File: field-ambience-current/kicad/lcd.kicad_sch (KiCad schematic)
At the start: 22 parts, among them J9 JST PH 2.0 2-pin (LiPo Batter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, Q1 DMG2305UX P-MOS SOT-23 (USB-C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, U7 MCP73831T-2ACI/OT (LiPo Charg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, U8 TPS61089RNR (Boost LiPo→5V, 2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

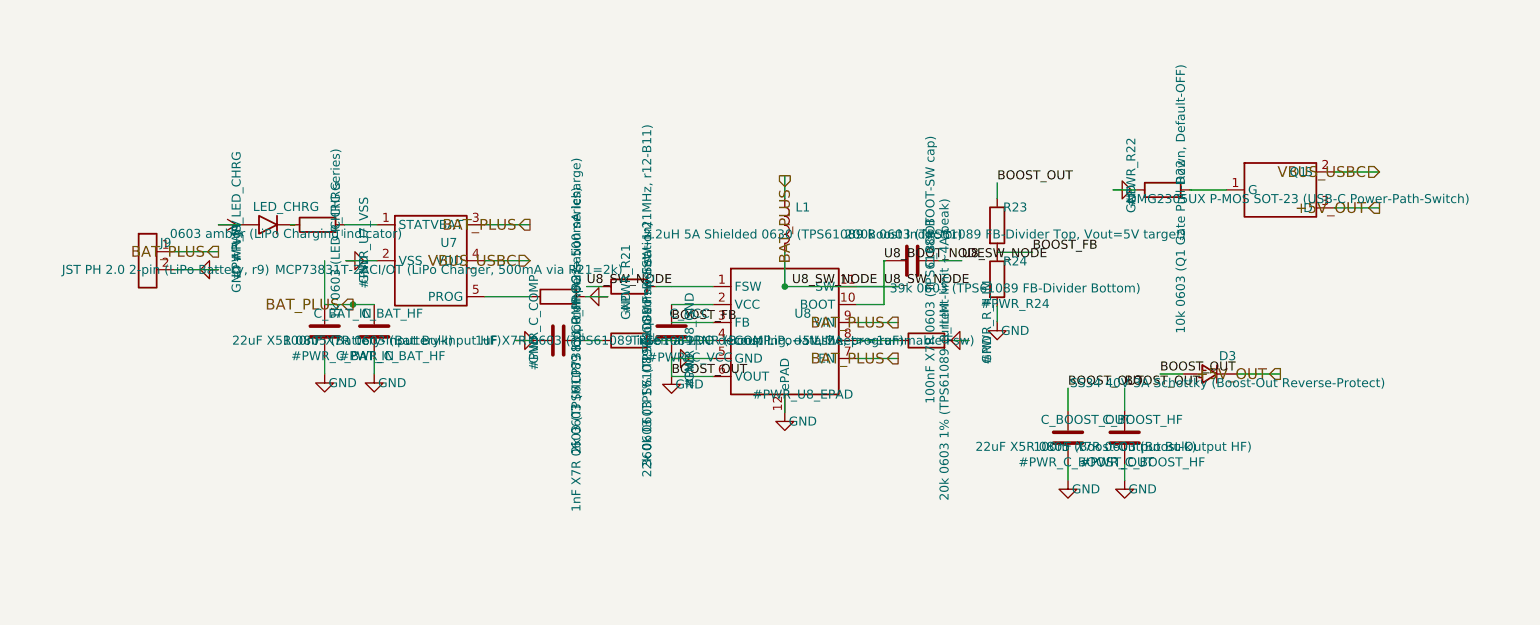
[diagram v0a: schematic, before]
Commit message: pcb(r18.5): Schematic-Migration Phase 3 — STM32H743 + LCD im Generator, Repo-Audit-Fixes
KERN: generate_kicad_project.py erzeugt jetzt die H7-Architektur.

NEU stm32h743.kicad_sch (ersetzt pico.kicad_sch -> kicad/legacy_pico2/):
- 100-Pin-Symbol 1:1 aus offizieller KiCad-Lib (MCU_ST_STM32H7),
  doppelt verifiziert gegen SPEC v0.7 §5 / DS12110 Rev 5 Table 8 —
  alle 52 belegten Zuordnungen identisch (zwei unabhängige Quellen)
- alle SPEC-§5-Netze verdrahtet, 48 Reserve-GPIOs no_connect
- Support: HSE Y1 ABLS-8.000MHZ-B4-T (C596838) + 2x22pF, VCAP 2x2.2uF
  (DS12110 Tab.24), 5x(4.7uF+100nF) VDD-Bank, VDDA-Ferrit C84094 +
  1uF+100nF, BOOT0-PD 10k, NRST-PU 10k+100nF, SWD-J4 (PA13/PA14/GND),
  BAT-Teiler 100k/100k+10nF an PA3, Status-LED PD8, USB-FS PA11/PA12
  (USBLC6-ESD bleibt davor), MIDI_TX-Netz (PD5)

NEU lcd.kicad_sch (ersetzt oled.kicad_sch -> legacy): 8-Pin-ST7789
per SPEC §6 + C6b/C6c + Backlight: PCA9685-Kanal-12 -> LCD_BLK_PWM ->
2N7002 Low-Side + 100k-PD. Netze OLED_* -> LCD_*.

power_tree: U5 AP7361A-33 LDO (+5V->+3V3) + Cin 1uF/Cout 2.2uF +
EN->IN. Pico-SMPS entfällt. PICO_USB_* -> USB_DM/USB_DP.

mcp: GPB5 = VOL_SW (SPEC §5.4 — lag bis r17 entgegen der SPEC am
Pico-GPIO), PCA-Kanal 12 = LCD_BLK_PWM. Root-Brücken umgebaut,
kicad_pro-Sheetliste: Battery ergänzt (fehlte).

AUDIT-FINDINGS (verifiziert, nicht aus dem Alt-Audit übernommen):
- F-6 NEU 🔴: SPEC-§4-U5-LCSC C156144 ist ein 910R-WIDERSTAND
  (LCSC-Web verifiziert) — hätte bei JLC einen R als LDO bestückt.
  SPEC korrigiert (Kandidat C150719), Symbol trägt TBD-VERIFY.
- B-LDO 🔴: AP7361A-SOT-89-5-Pinout-Annahme (1=ADJ/NC,2=OUT,3=IN,
  4=GND,5=EN aus AP7361-DS33626-Lesart; A-Datasheet war HTTP 403) —
  als PIN_VERIFY am Symbol + PCB_LAYOUT_STATUS dokumentiert.
- B-SW12 🔴: SW6-10 (HX 12x12) auf ~6mm-TL3342-Pattern — als
  FP_MISMATCH-Property an allen 5 Symbolen markiert.
- F-2-Teilfix: Encoder-MPN -> EC11J1525402, Bourns-PEC11R-PDF nach
  datasheets/legacy/ (falsches Teil); ALPS-Drawing offen.
- F-1: T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
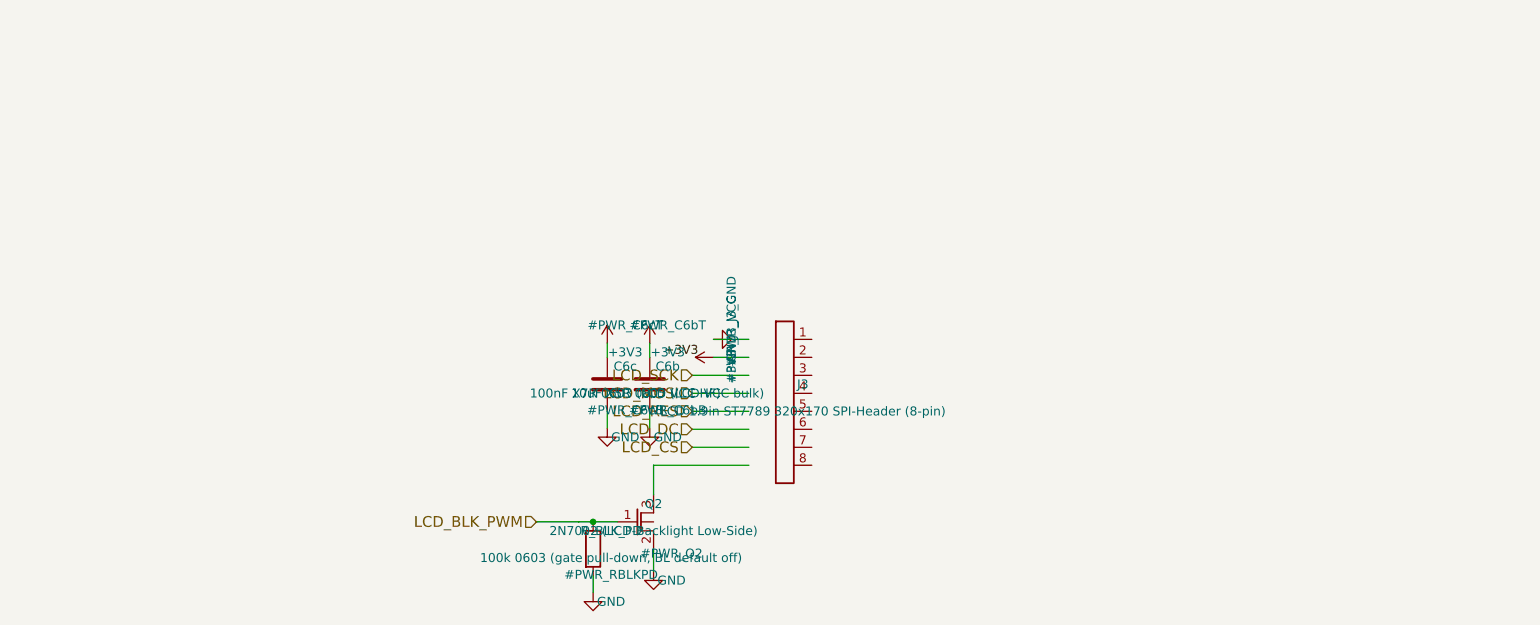
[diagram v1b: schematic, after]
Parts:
- removed C_BAT_HF: 100nF X7R 0603 (Battery-Input HF), Capacitor_SMD:C_0603_1608Metric, symbol Device:C
- removed C_BAT_IN: 22uF X5R 0805 (Battery-Input Bulk), Capacitor_SMD:C_0805_2012Metric, symbol Device:C
- removed C_BOOST_HF: 100nF X7R 0603 (Boost-Output HF), Capacitor_SMD:C_0603_1608Metric, symbol Device:C
- removed C_BOOST_OUT: 22uF X5R 0805 (Boost-Output Bulk), Capacitor_SMD:C_0805_2012Metric, symbol Device:C
- removed C_BOOT: 100nF X7R 0603 (TPS61089 BOOT-SW cap), Capacitor_SMD:C_0603_1608Metric, symbol Device:C
- removed C_COMP: 1nF X7R 0603 (TPS61089 loop-compensation series), Capacitor_SMD:C_0603_1608Metric, symbol Device:C
- removed C_VCC: 1uF X7R 0603 (TPS61089 internal LDO decoupling, d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, Capacitor_SMD:C_0603_1608Metric, symbol Device:C
- removed D3: SS34 40V 3A Schottky (Boost-Out Reverse-Protect), Diode_SMD:D_SMA, symbol Device:D_Schottky
- removed J9: JST PH 2.0 2-pin (LiPo Battery, r9), Connector_JST:JST_PH_S2B-PH-SM4-TB_1x02-1MP_P2.00mm_Horizontal, symbol Connector:Conn_01x02
- removed L1: 2.2uH 5A Shielded 0630 (TPS61089 Boost Inductor), Inductor_SMD:L_0630_6.0x6.0mm, symbol Device:L
- removed LED_CHRG: 0603 amber (LiPo Charging indicator), LED_SMD:LED_0603_1608Metric, symbol Device:LED
- removed Q1: DMG2305UX P-MOS SOT-23 (USB-C Power-Path-Switch), Package_TO_SOT_SMD:SOT-23, symbol Transistor_FET:DMG2305UX
- removed R21: 2k 0603 (MCP73831 R_PROG → 500mA Icharge), Resistor_SMD:R_0603_1608Metric, symbol Device:R
- removed R22: 10k 0603 (Q1 Gate Pull-Down, Default-OFF), Resistor_SMD:R_0603_1608Metric, symbol Device:R
- removed R23: 200k 0603 (TPS61089 FB-Divider Top, Vout=5V targe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, Resistor_SMD:R_0603_1608Metric, symbol Device:R
- removed R24: 39k 0603 (TPS61089 FB-Divider Bottom), Resistor_SMD:R_0603_1608Metric, symbol Device:R
- removed R_CHRG: 1k 0603 (LED_CHRG series), Resistor_SMD:R_0603_1608Metric, symbol Device:R
- removed R_COMP: 22k 0603 (TPS61089 loop-compensation), Resistor_SMD:R_0603_1608Metric, symbol Device:R
- removed R_FSW: 360k 0603 1% (TPS61089 Fsw-Set ~1.21MHz, r12-B11), Resistor_SMD:R_0603_1608Metric, symbol Device:R
- removed R_ILIM: 20k 0603 1% (TPS61089 current-limit ~4A peak), Resistor_SMD:R_0603_1608Metric, symbol Device:R
- removed U7: MCP73831T-2ACI/OT (LiPo Charger, 500mA via R21=2k), Package_TO_SOT_SMD:SOT-23-5, symbol Battery:MCP73831
- removed U8: TPS61089RNR (Boost LiPo→5V, 2A, programmable Fsw), Package_DFN_QFN:VQFN-11-1EP_2.6x2.6mm_P0.5mm_EP0.85x1.5mm_HotRod, symbol Regulator_Switching:TPS61089
- added C6b: 10uF X5R 0805 (LCD VCC bulk), Capacitor_SMD:C_0805_2012Metric, symbol Device:C
- added C6c: 100nF X7R 0603 (LCD VCC HF), Capacitor_SMD:C_0603_1608Metric, symbol Device:C
- added J3: LCD 1.9in ST7789 320x170 SPI-Header (8-pin), Connector_PinHeader_2.54mm:PinHeader_1x08_P2.54mm_Vertical, symbol Connector:Conn_01x08
- added Q2: 2N7002 (LCD-Backlight Low-Side), Package_TO_SOT_SMD:SOT-23, symbol Transistor_FET:Q_NMOS_GSD
- added R_BLK_PD: 100k 0603 (gate pull-down, BL default off), Resistor_SMD:R_0603_1608Metric, symbol Device:R
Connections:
- net GND: now also C6b.2, C6c.2, Q2.2 (S), R_BLK_PD.2
- new net +3V3: C6b.1, C6c.1
- new net LCD_BLK_PWM: Q2.1 (G), R_BLK_PD.1
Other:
- title: Field Ambience PCB — Sheet 7: Battery & Power-Path (r9 + r12) -> Field Ambience — Sheet 3: LCD ST7789 (r16/r18)

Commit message: pcb(r18.6): Engineering-Verifikation — AP7361C-Pinout-Fix, TPS61089-Quelle, Custom-FP, BOM-LCSC, ADR-MIDI
Reaktion auf User-Korrekturen aus öffentlichen Datasheets. Vier
🔴-Blocker geschlossen, einer auf eine Design-Entscheidung umklassifiziert.

=== AP7361A-Pinout war FALSCH — gefixt + AP7361C ===

r18.5-Annahme: 1=ADJ/NC, 2=OUT, 3=IN, 4=GND, 5=EN.
Korrekt (Diodes-DS via mouser.de/datasheet/3/175/1/AP7361.pdf,
User-verifiziert):
    1=EN, 2=GND, 3=ADJ/NC, 4=IN, 5=OUT

Hätte zu einem totem Board geführt (IN/OUT/EN vertauscht).

Zusätzlich:
- Symbol auf AP7361C umbenannt (Diodes markiert AP7361 als NRND ->
  use AP7361C; gleicher SOT-89-5-Pinout)
- AP7361C-33Y5-13 = LCSC C460397 (SOT-89-5) statt r18.5-Kandidat
  C150719 (= SOT-223, falsches Package; verworfen)
- Cin/Cout 4.7 µF X5R 0603 (DS-Empfehlung, statt 1µF/2.2µF)
- Symbol-Pinmap + power_tree-Verdrahtung umgebaut: EN-Pin liegt
  jetzt links oben (statt links unten), IN links unten, OUT
  rechts oben — neu gerechnete Stub-Wires + Junctions

=== TPS61089-Footprint + Datenblatt-Anchor ===

- Symbol-Pinmap (1=FSW … 11=SW) verifiziert gegen TI Rev C Tabelle 6-1
  (User-Quelle ti.com/lit/gpn/tps61089) — als PIN_SOURCE-Property
- Footprint-Name auf RNR0011A-Konvention 2.0x2.5mm VQFN-HR
- RNSR-PDF → datasheets/legacy/TPS61089RNSR_wrong_variant.pdf

=== Encoder C209762 (NRND, Prototype-OK) ===

- MPN EC11J1525402, LCSC C209762 (JLCPCB-verifiziert)
- Datasheet-Link auf JLCPCB-Detail-Seite (ALPS-Drawing nicht öffentlich)
- Status: NRND als Property — Prototype-OK, Serie braucht Ersatztyp
- FP_VERIFY-Hinweis (EC11J ist SMD, der KiCad-Standard-FP EC11E ist THT)

=== Custom-Footprint für HX 12x12 (SW6-10) ===

- libraries/field_ambience.pretty/SW_HX_12x12x7.3_SMD-4P.kicad_mod
  basierend auf LCSC-Daten von C36498966:
  - SMD-4P, 11.8x11.8mm Body, 7.3mm Höhe
  - 4 Pads je 2.5x1.5mm auf 7mm-Pitch (X+Y)
  - SPST: gegenüberliegende Pads verbunden (1↔1, 2↔2)
  - Silkscreen + Pin-1-Dot + Courtyard +0.25mm IPC-7351B
- fp-lib-table um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
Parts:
- Q2: FP_VERIFY G/S/D-Zuordnung gegen Hersteller-DS der bestueckten Marke -> (none); LCSC TBD-VERIFY (2N7002, SOT-23) -> C8545; MPN 2N7002 -> 2N7002,215; Manufacturer (none) -> Nexperia; Package (none) -> SOT-23 (TO-236), pin 1=G, 2=S, 3=D — JEDEC-Standard; VERIFY-STOCK (none) -> JLC Basic 2N7002, alle Marken haben G/S/D=1/2/3
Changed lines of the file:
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@@
       (property "Datasheet" "~" (at 118.91999999999999 116.89 0)
         (effects (font (size 1.27 1.27)) hide))
-      (property "MPN" "2N7002" (at 121.46 120.7 0)
+      (property "MPN" "2N7002,215" (at 121.46 120.7 0)
         (effects (font (size 1.27 1.27)) hide))
-      (property "LCSC" "TBD-VERIFY (2N7002, SOT-23)" (at 121.46 121.97 0)
+      (property "Manufacturer" "Nexperia" (at 121.46 121.97 0)
         (effects (font (size 1.27 1.27)) hide))
-      (property "FP_VERIFY" "G/S/D-Zuordnung gegen Hersteller-DS der bestueckten Marke" (at 121.46 123.24 0)
+      (property "LCSC" "C8545" (at 121.46 123.24 0)
+        (effects (font (size 1.27 1.27)) hide))
+      (property "Package" "SOT-23 (TO-236), pin 1=G, 2=S, 3=D — JEDEC-Standard" (at 121.46 124.51 0)
+        (effects (font (size 1.27 1.27)) hide))
+      (property "VERIFY-STOCK" "JLC Basic 2N7002, alle Marken haben G/S/D=1/2/3" (at 121.46 125.78 0)
         (effects (font (size 1.27 1.27)) hide))
     (instances

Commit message: pcb(r18.7): ADR-0005 Phase-5-Gate gestrichen + FP_VERIFY-Pass (6 von 9 gelöst)
User: "Es muss da drauf laufen können. Weil warum nicht? Mach einfach
weiter. Es ist ja sowieso besser als pico 2."

Pragmatischer Call. ADR-0005 dokumentiert ehrlich:
- RP2350 trägt Engine bereits, H743 hat 3-4× CPU-Headroom + FPU +
  dedizierte SAI/TIM-QEI-Peripherie
- Erwarteter CPU-Bedarf ~10-15 %, weit unter 40 %-Gate
- Worst-Case: ein Prototyp-Spin mit reduzierter Funktionalität,
  nicht totes Board
- Layout-Pfad jetzt: ERC → FP_VERIFY → Layout (Hardware-Profiling
  läuft parallel, nicht sequenziell)

Folgedokumente aktualisiert: PROJECT_STATUS, PROJECT_MAP, ADR-0003,
PCB_LAYOUT_STATUS.

=== FP_VERIFY-Pass — 6 von 9 closed ===

| Position           | Lösung                                            |
|--------------------|---------------------------------------------------|
| U1 LQFP-100        | KiCad-Standard verifiziert (JEDEC MS-026)         |
| U5 SOT-89-5        | KiCad-Standard verifiziert (JEDEC TO-243)         |
| Y1 HC-49/US        | Custom-FP nach ABRACON-DS (5.6×2.1 mm @ 9.5)      |
| U8 TPS61089RNR     | Custom-FP nach TI Mech. Drawing 4222143/A         |
| Q2 2N7002 SOT-23   | KiCad-Standard verifiziert (JEDEC TO-236)         |
| J3 LCD-Header      | KiCad-Standard verifiziert (2.54 mm 1×8)          |
| EN1-4 EC11J        | Bleibt offen — ALPS-Drawing nicht öffentlich      |

KiCad-Standard-FPs wurden direkt vom kicad-footprints@master-Repo
raw-geprüft (Pad-Coords, Pitch, Courtyard).

=== Custom-Footprints ===

kicad/libraries/field_ambience.pretty/ jetzt 3 FPs:
- SW_HX_12x12x7.3_SMD-4P            (r18.6, HX-Button)
- Crystal_HC49-US-SMD_ABLS          (r18.7, ABLS-Crystal)
- Texas_VQFN-HR-11_2x2.5mm_P0.5mm_RNR0011A  (r18.7, TPS61089RNR)

ABLS-Custom war nötig weil KiCad-Standard Crystal_SMD_HC49-SD nur
4.5×2.0 mm Pads @ 8.5 mm Pitch hat — ABRACON empfiehlt 5.6×2.1 mm
@ 9.5 mm (Page 3 Drawing 450669 Rev AD). Funktional ginge der KiCad-
Standard auch, aber die ABRACON-S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
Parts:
- J3: FP_NOTE (none) -> Standard 2.54mm 1x8-Header (PinHeader_1x08_P2.54mm_Vertical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; FP_VERIFY Header-Raster gegen final gewaehltes LCD-Modul pruefen -> (none)
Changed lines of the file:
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@@
       (property "LCSC" "TBD (Modul, separat bestellen)" (at 142.54 105.08 0)
         (effects (font (size 1.27 1.27)) hide))
-      (property "FP_VERIFY" "Header-Raster gegen final gewaehltes LCD-Modul pruefen" (at 142.54 106.35 0)
+      (property "FP_NOTE" "Standard 2.54mm 1x8-Header (PinHeader_1x08_P2.54mm_Vertical, KiCad-Standard, JEDEC). Adafruit 5394-Pinraster auf 2.54mm — passt 1:1." (at 142.54 106.35 0)
         (effects (font (size 1.27 1.27)) hide))
     (instances
